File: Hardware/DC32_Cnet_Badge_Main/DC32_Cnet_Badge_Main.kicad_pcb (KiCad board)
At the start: 2 copper layers, 230 x 138 mm, 22 parts, among them J1 SAO_Conn, J3 Conn_01x02_Male, U2 MH-CD42_LiPo_Batery_Managemen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

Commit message: Incremental Commit
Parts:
- added REF**: DC32 Logo, DC32_Cnet_Badge_Main:DC32 Logo, B.Cu at (102.0, 93.0)
- moved Ref** 3.16 mm to (113.0, 101.0)
- moved Ref** 2.00 mm to (72.0, 73.0)
- moved Ref** 1.41 mm to (227.0, 80.0)

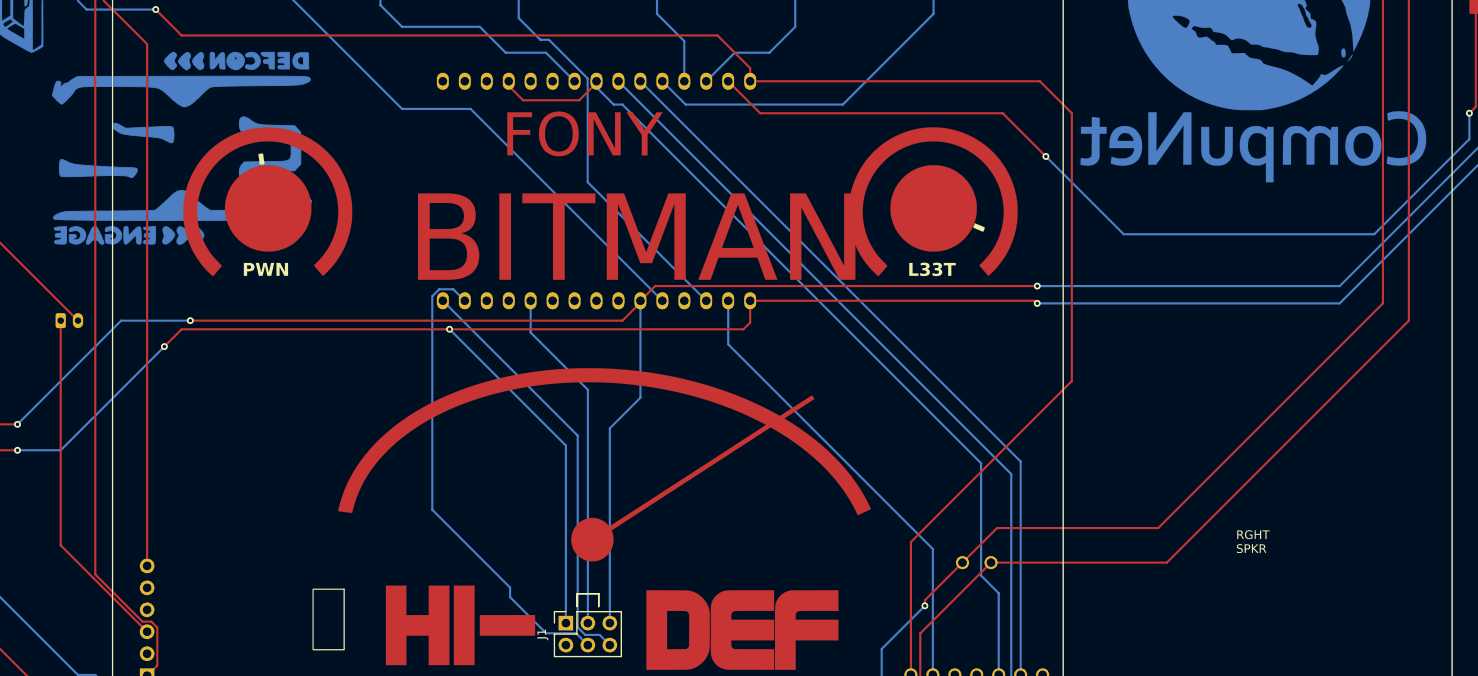
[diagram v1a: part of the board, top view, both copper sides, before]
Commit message: Reverted to ESP32 2.0.12
ESP32 2.0.14 has issues with Bluetooth signal quality.
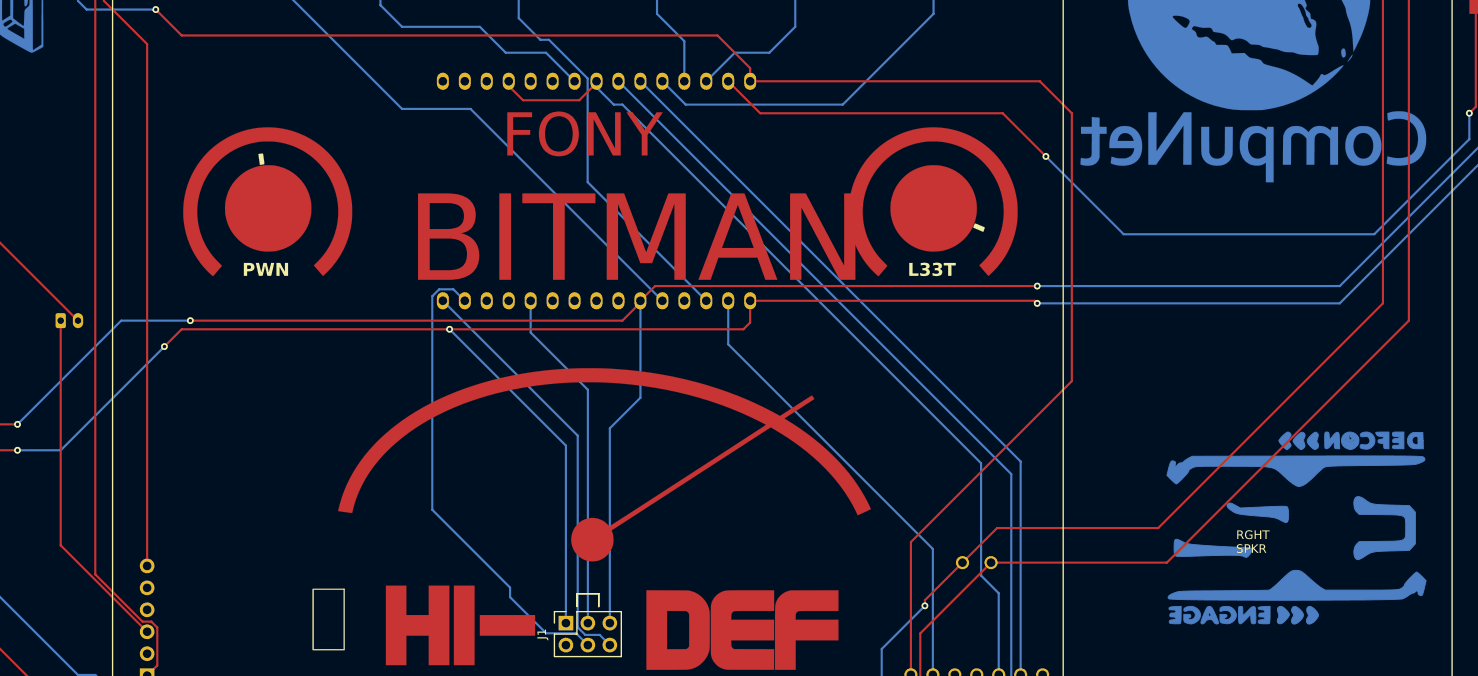
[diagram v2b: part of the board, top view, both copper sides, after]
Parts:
- moved REF** 136.3 mm to (231.0, 136.9)
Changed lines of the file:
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@@
   )
   (footprint "DC32_Cnet_Badge_Main:DC32 Logo" (layer "B.Cu")
-    (at 102 93 180)
+    (at 230.974068 136.939772 180)
     (attr smd)
     (fp_text reference "REF**" (at 0 0.5 unlocked) (layer "B.SilkS") hide

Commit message: PCB updates
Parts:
- moved Ref** 32.2 mm to (98.0, 92.0)
- moved REF** 3.61 mm to (228.0, 134.9)
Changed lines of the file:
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@@
     (property "Sheetname" "")
     (attr through_hole)
-    (fp_text reference "S1" (at 9.525 5.969 90) (layer "B.SilkS")
+    (fp_text reference "S1" (at 4 9 -180) (layer "B.SilkS")
         (effects (font (size 1.4 1.4) (thickness 0.15)) (justify mirror))
     )
@@
   )
   (footprint "DC32_Cnet_Badge_Main:defcon31-logo" (layer "B.Cu")
-    (at 72 73 180)
+    (at 98 92 180)
     (attr through_hole)
     (fp_text reference "Ref**" (at 0 0) (layer "B.SilkS") hide
@@
   )
   (footprint "DC32_Cnet_Badge_Main:DC32 Logo" (layer "B.Cu")
-    (at 230.974068 136.939772 180)
+    (at 227.974068 134.939772 180)
     (attr smd)
     (fp_text reference "REF**" (at 0 0.5 unlocked) (layer "B.SilkS") hide
